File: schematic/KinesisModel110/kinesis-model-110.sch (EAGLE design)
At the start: 25 parts, among them IC1 MEGA16-A, IC2 74LS138N, IC3 74LS138N, IC4 AT24CP, Q1 16mhz

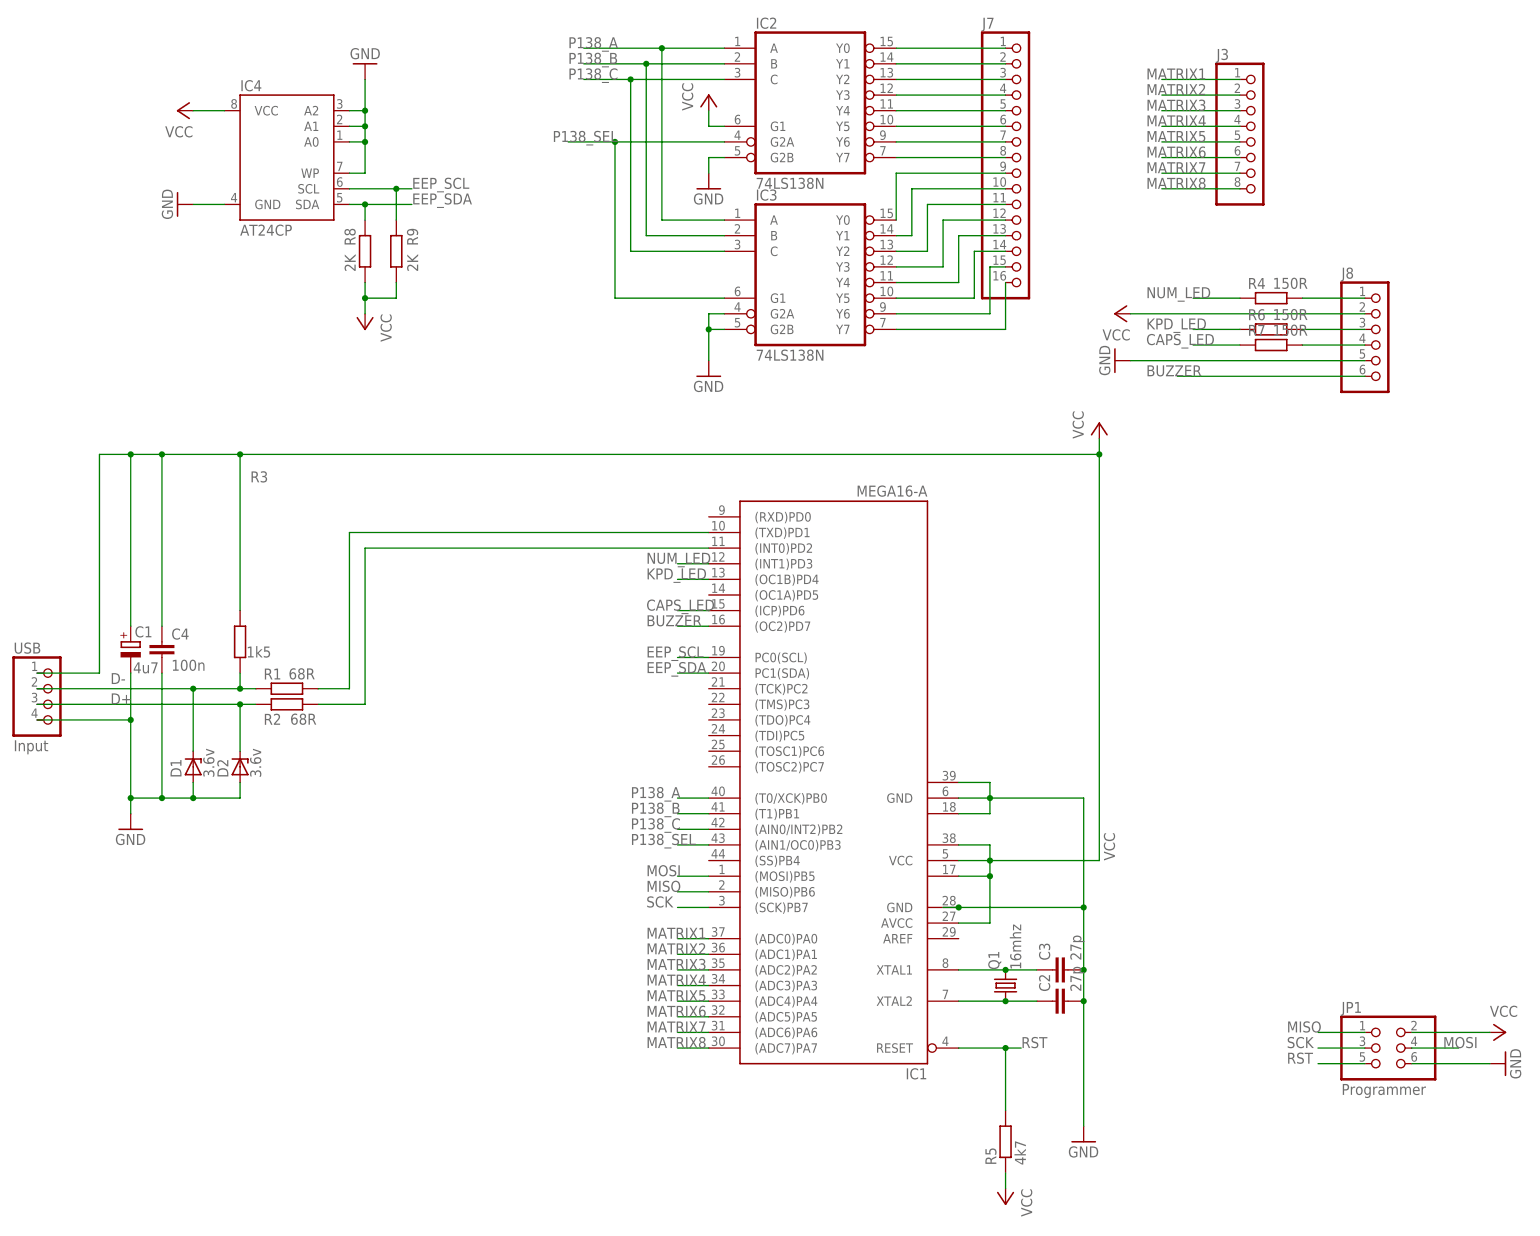
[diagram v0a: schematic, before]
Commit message: Redesign Kinesis Model 110 PCB for 2-layer manufacturing
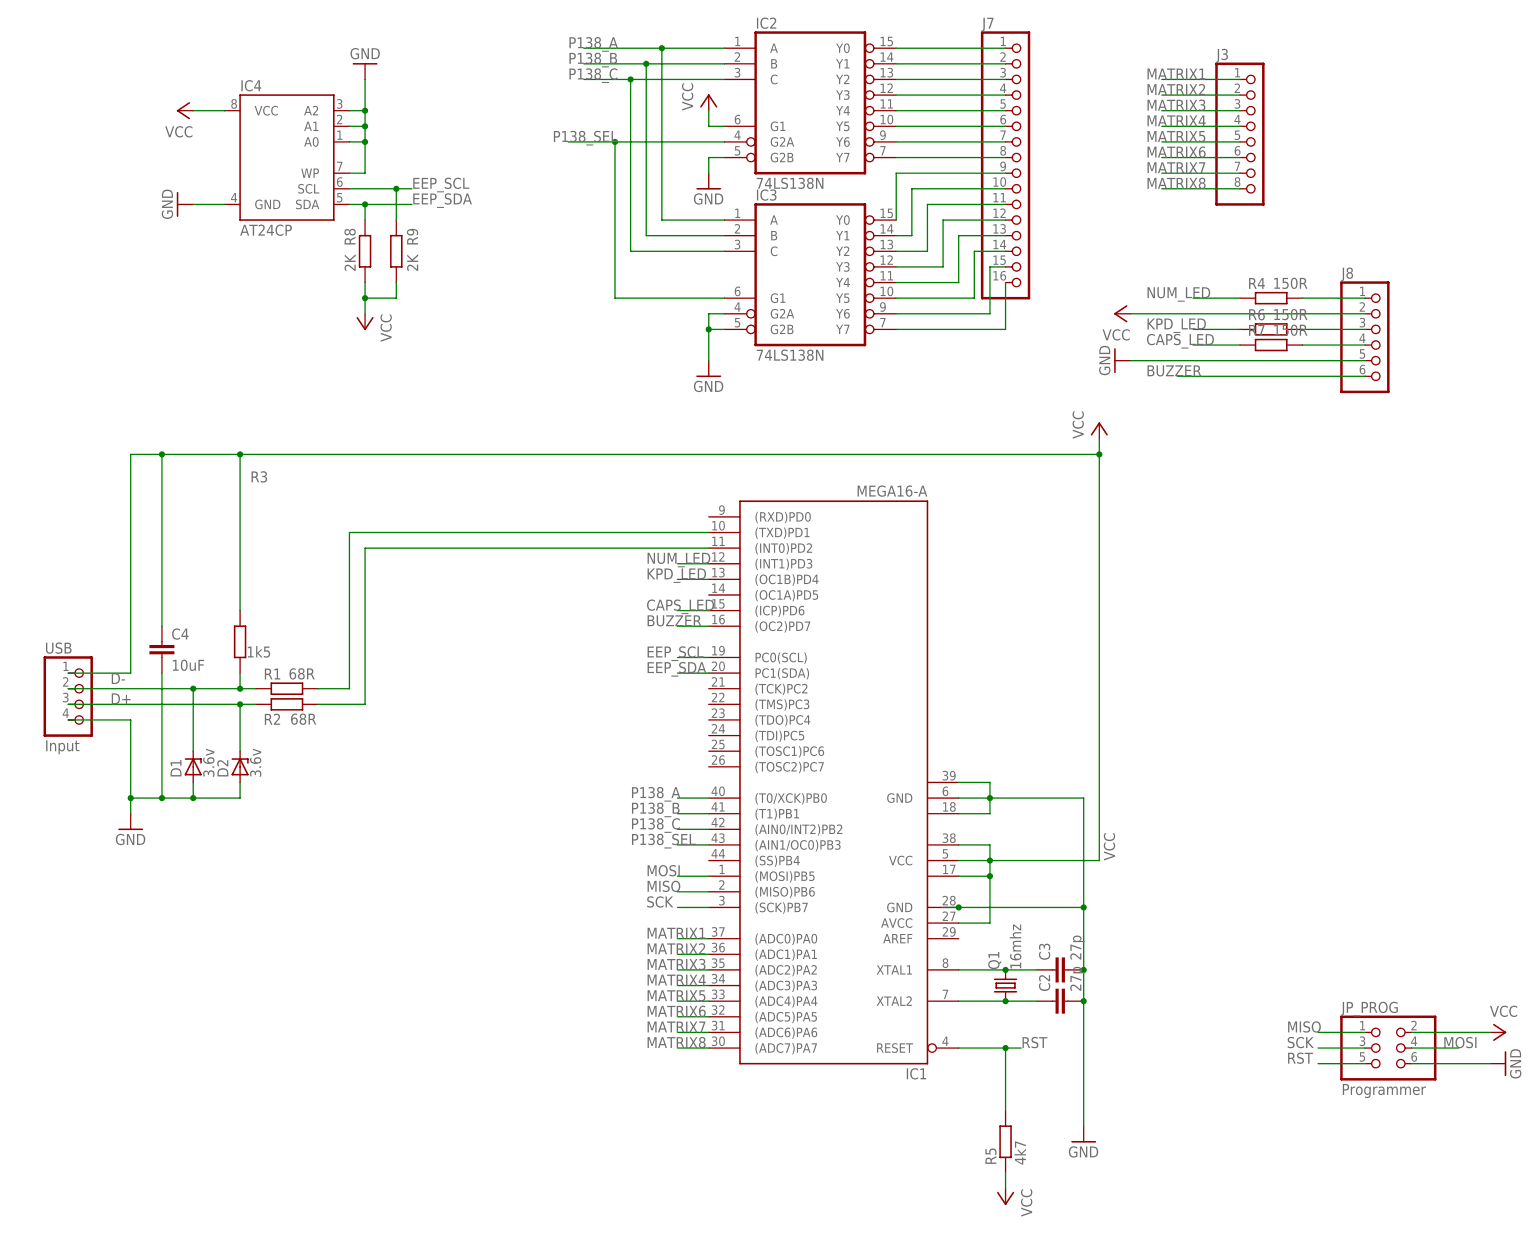
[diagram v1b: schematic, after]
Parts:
- removed C1: 4u7, rcl:CPOL-EUE2-5
- C2, C3: device rcl:C-EUC0805 -> rcl:C-EUC0603
- C4: value 100n -> 10uF
- R1, R2, R3, R4, R5, R6, R7, R8, R9: device rcl:R-EU_R0805 -> rcl:R-EU_R0603
- renumbered JP1 to JP_PROG
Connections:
- net GND: no longer C1.-
- net VCC: no longer C1.+
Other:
- moved on the sheet: USB
